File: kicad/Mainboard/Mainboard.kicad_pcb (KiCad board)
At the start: 2 copper layers, 46.9 x 107.1 mm, 273 parts, among them J1 ESP8266 module, J10 MIC_EXT, J11 VIB2, J12 SPK_EXT, J13 GPS_CONN, J14 Micro_SD_Card, J15 DBG_CONN, J3 USB_OTG, J4 SWD, J5 BATT, J6 POT_PWR_SW, J7 Conn_01x10, J8 Antenna, J9 VIB1, Q1 BSS138, Q2 BSS138, Q3 BGA6589, Q4 BSS138, Q5 BSS138, Q6 BSS138, Q7 FDV304P, SW1 INT_PTT_SW, T1 AFT05MS004NT1, U1 STM32F777VIT, U10 LM386, U11 LSM9DS1, U13 BGA2874, U2 USBLC6-2SC6, U3 LD1117S50TR_SOT223, U4 LD1117S33TR_SOT223, U5 ADF7021, U6 HMC546MS8GETR, U7 LM2904A, U8 HEF4066B, U9 OPA340UA, X1 12.288MHz

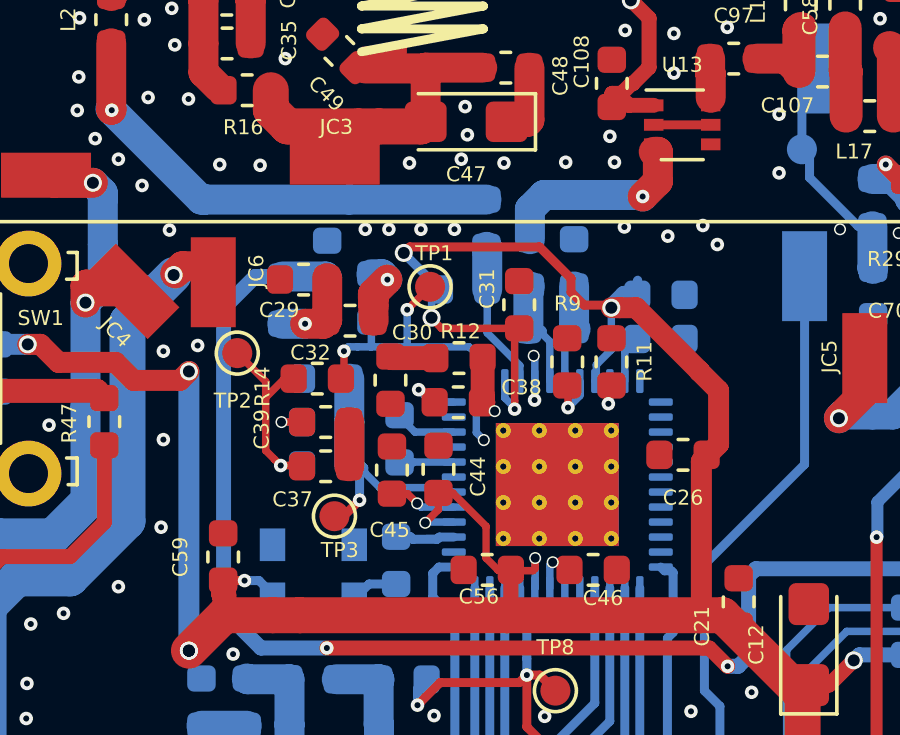
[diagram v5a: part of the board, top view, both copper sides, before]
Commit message: more changes on RF chipset - adding jumperpoint 15&16
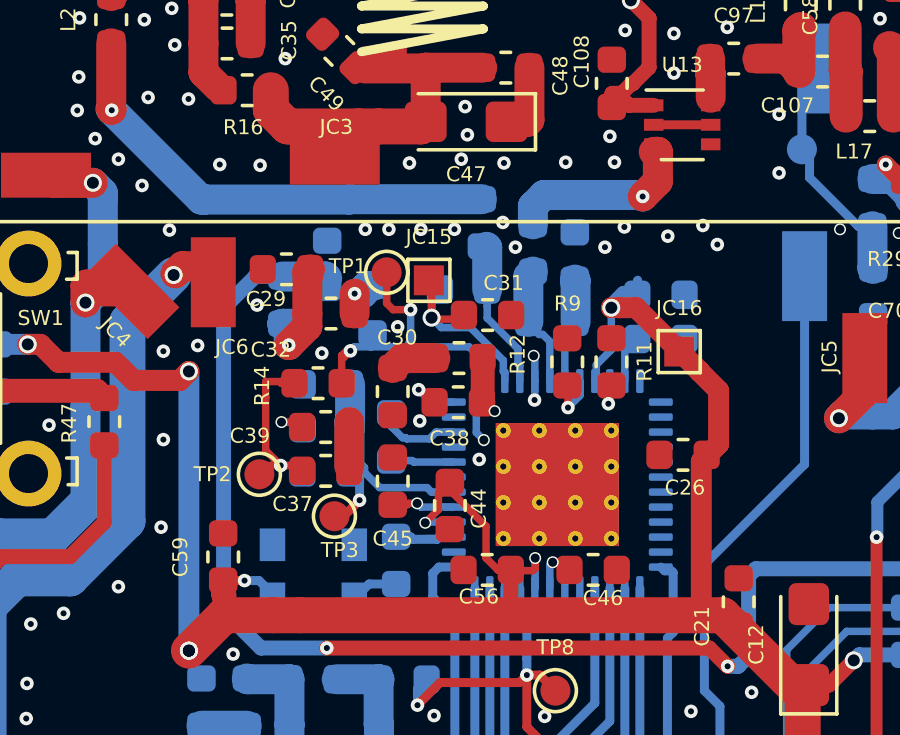
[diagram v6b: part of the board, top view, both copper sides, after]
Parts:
- added JC15: 3,3V, TestPoint:TestPoint_Pad_1.0x1.0mm, F.Cu at (36.0, 96.1)
- added JC16: 3,3V, TestPoint:TestPoint_Pad_1.0x1.0mm, F.Cu at (44.3, 98.4)
- moved TP2 4.11 mm to (30.3, 102.5)
- moved TP1 1.53 mm to (34.5, 95.8)
- moved C44 1.27 mm to (36.7, 103.6), turned to 270 degrees
- moved C31 1.11 mm to (37.9, 97.2), turned to 0 degrees
- moved C32 0.68 mm to (32.7, 97.2)
- moved C29 0.67 mm to (31.2, 95.7)
- moved C23 0.51 mm to (39.4, 95.0)
- moved R13 0.40 mm to (34.1, 97.0)
- moved C30 0.39 mm to (34.7, 99.8)
- moved C45 0.37 mm to (34.7, 102.8)
- moved L14 0.29 mm to (34.7, 101.3)
- moved L4 0.24 mm to (40.1, 97.4)
- moved C25 0.23 mm to (40.8, 95.2)
- moved R15 0.23 mm to (32.5, 102.5)
- moved R17 0.20 mm to (32.5, 101.0)
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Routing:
- net +3V3: track 448.1 -> 437.4 mm, vias 34 -> 32
- net Net-(C29-Pad2): track 2.95 -> 4.38 mm
- net Net-(C32-Pad1): track 2.50 -> 1.17 mm
- net Net-(L14-Pad1): track 1.66 -> 2.79 mm
- net Net-(L14-Pad2): track 1.43 -> 2.11 mm
- net Net-(R13-Pad1): track 11.8 -> 12.5 mm
- net Net-(C22-Pad2): track 5.49 -> 4.94 mm
- net RX: track 6.82 -> 6.28 mm
- net GND: vias 337 -> 345

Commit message: more changes
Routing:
- net GND: vias 345 -> 346
- net (no net): vias 1 -> 0
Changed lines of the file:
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@@
     (effects (font (size 0.7 0.7) (thickness 0.175)) (justify mirror))
   )
-  (via (at 51.3715 82.5119) (size 0.45) (drill 0.2) (layers F.Cu B.Cu) (net 0))
+  (via (at 51.3715 82.5119) (size 0.45) (drill 0.2) (layers F.Cu B.Cu) (net 1))
   (via (at 38.4175 94.1324) (size 0.45) (drill 0.2) (layers F.Cu B.Cu) (net 1) (status 40000))
   (via (at 38.8366 94.9579) (size 0.45) (drill 0.2) (layers F.Cu B.Cu) (net 1) (status 40000))

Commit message: added new PCB photos
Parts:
- moved JC12 5.58 mm to (50.1, 94.5)
- moved JC14 2.31 mm to (46.8, 98.3)
- moved TP7 0.44 mm to (48.4, 91.2)
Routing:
- net Net-(JC11-Pad1): track 13.5 -> 11.0 mm
- net TRX_SW: track 68.4 -> 66.1 mm
- net +BATT: track 180.5 -> 181.5 mm
- net GND: vias 346 -> 378
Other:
- board text added: "Pcb by: Nikoloz SO3ALG"
- board text added: "Schematic by: Wojtek SP5WWP, Mathis DB9MAT et al."
- board text removed: "Pcb by: Nikoloz SO3ALG Wojciech SP5WWP"
